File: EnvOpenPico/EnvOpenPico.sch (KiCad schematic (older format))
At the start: 53 parts, among them J2 SKRKAEE020, J3 2.54mm header 01x20, J4 2.54mm header 01x20, J5 Conn_01x03_Male, U1 TPS63002, U3 RP2040, Y1 Crystal

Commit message: added keepout zones around the pins to avoid shorts
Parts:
- Y1: footprint Crystal:Crystal_SMD_5032-2Pin_5.0x3.2mm -> Crystal:Crystal_SMD_3225-4Pin_3.2x2.5mm; symbol Device:Crystal -> Device:Crystal_GND24
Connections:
- wire segments 220 -> 221
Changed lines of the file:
@@
 Connection ~ 3700 5550
 $Comp
-L Device:Crystal Y1
+L Device:Crystal_GND24 Y1
 U 1 1 612055A1
 P 3200 8650
-F 0 "Y1" V 3154 8781 50  0000 L CNN
-F 1 "Crystal" V 3245 8781 50  0000 L CNN
-F 2 "Crystal:Crystal_SMD_5032-2Pin_5.0x3.2mm" H 3200 8650 50  0001 C CNN
+F 0 "Y1" V 3200 8600 50  0000 L CNN
+F 1 "Crystal" V 3400 8700 50  0000 L CNN
+F 2 "Crystal:Crystal_SMD_3225-4Pin_3.2x2.5mm" H 3200 8650 50  0001 C CNN
 F 3 "~" H 3200 8650 50  0001 C CNN
 	1    3200 8650
@@
 	0    -1   -1   0
 $EndComp
-$Comp
-L power:GND #PWR019
-U 1 1 61280CDE
-P 3200 9250
-F 0 "#PWR019" H 3200 9000 50  0001 C CNN
-F 1 "GND" H 3205 9077 50  0000 C CNN
-F 2 "" H 3200 9250 50  0001 C CNN
-F 3 "" H 3200 9250 50  0001 C CNN
-	1    3200 9250
-	1    0    0    -1
-$EndComp
 Wire Wire Line
 	3200 8400 3950 8400
@@
 Wire Wire Line
 	2550 8650 2550 8400
+$Comp
+L power:GND #PWR?
+U 1 1 611FF3FA
+P 3400 8650
+F 0 "#PWR?" H 3400 8400 50  0001 C CNN
+F 1 "GND" V 3405 8522 50  0000 R CNN
+F 2 "" H 3400 8650 50  0001 C CNN
+F 3 "" H 3400 8650 50  0001 C CNN
+	1    3400 8650
+	0    -1   -1   0
+$EndComp
+Wire Wire Line
+	2550 8650 3000 8650
 $EndSCHEMATC

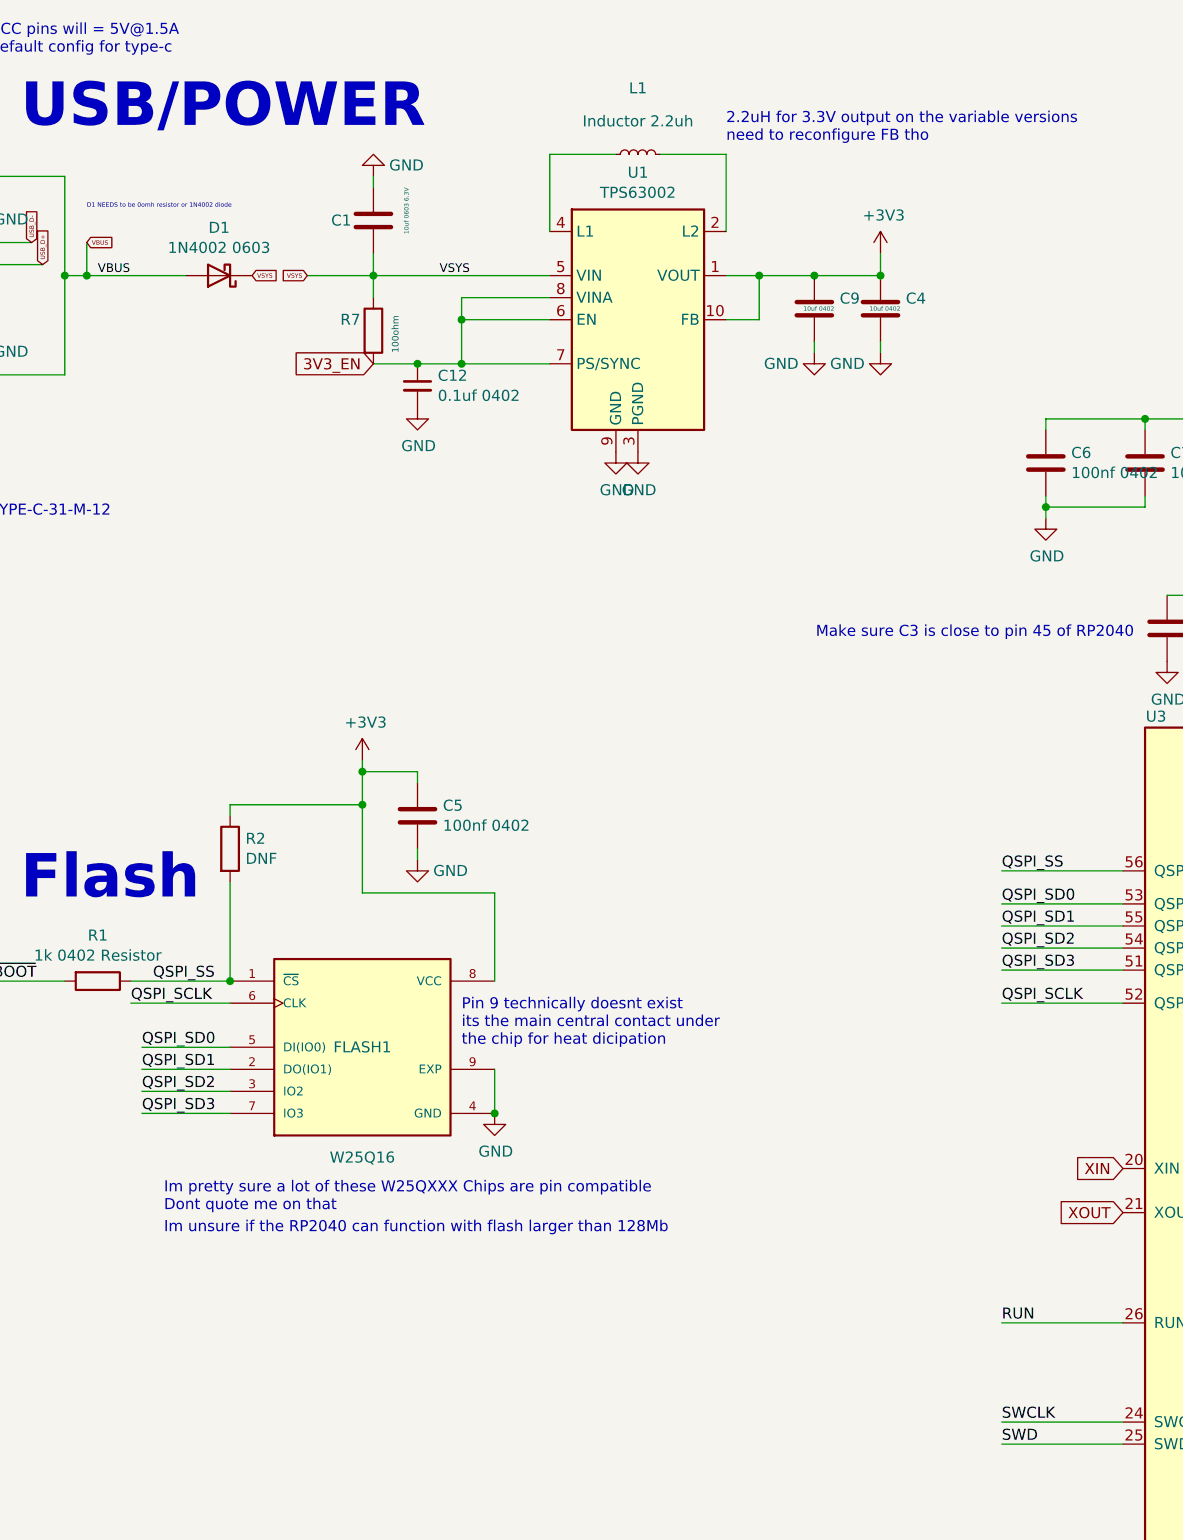
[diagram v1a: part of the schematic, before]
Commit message: Added Reset button + general other tweaks, cleanups and changes.
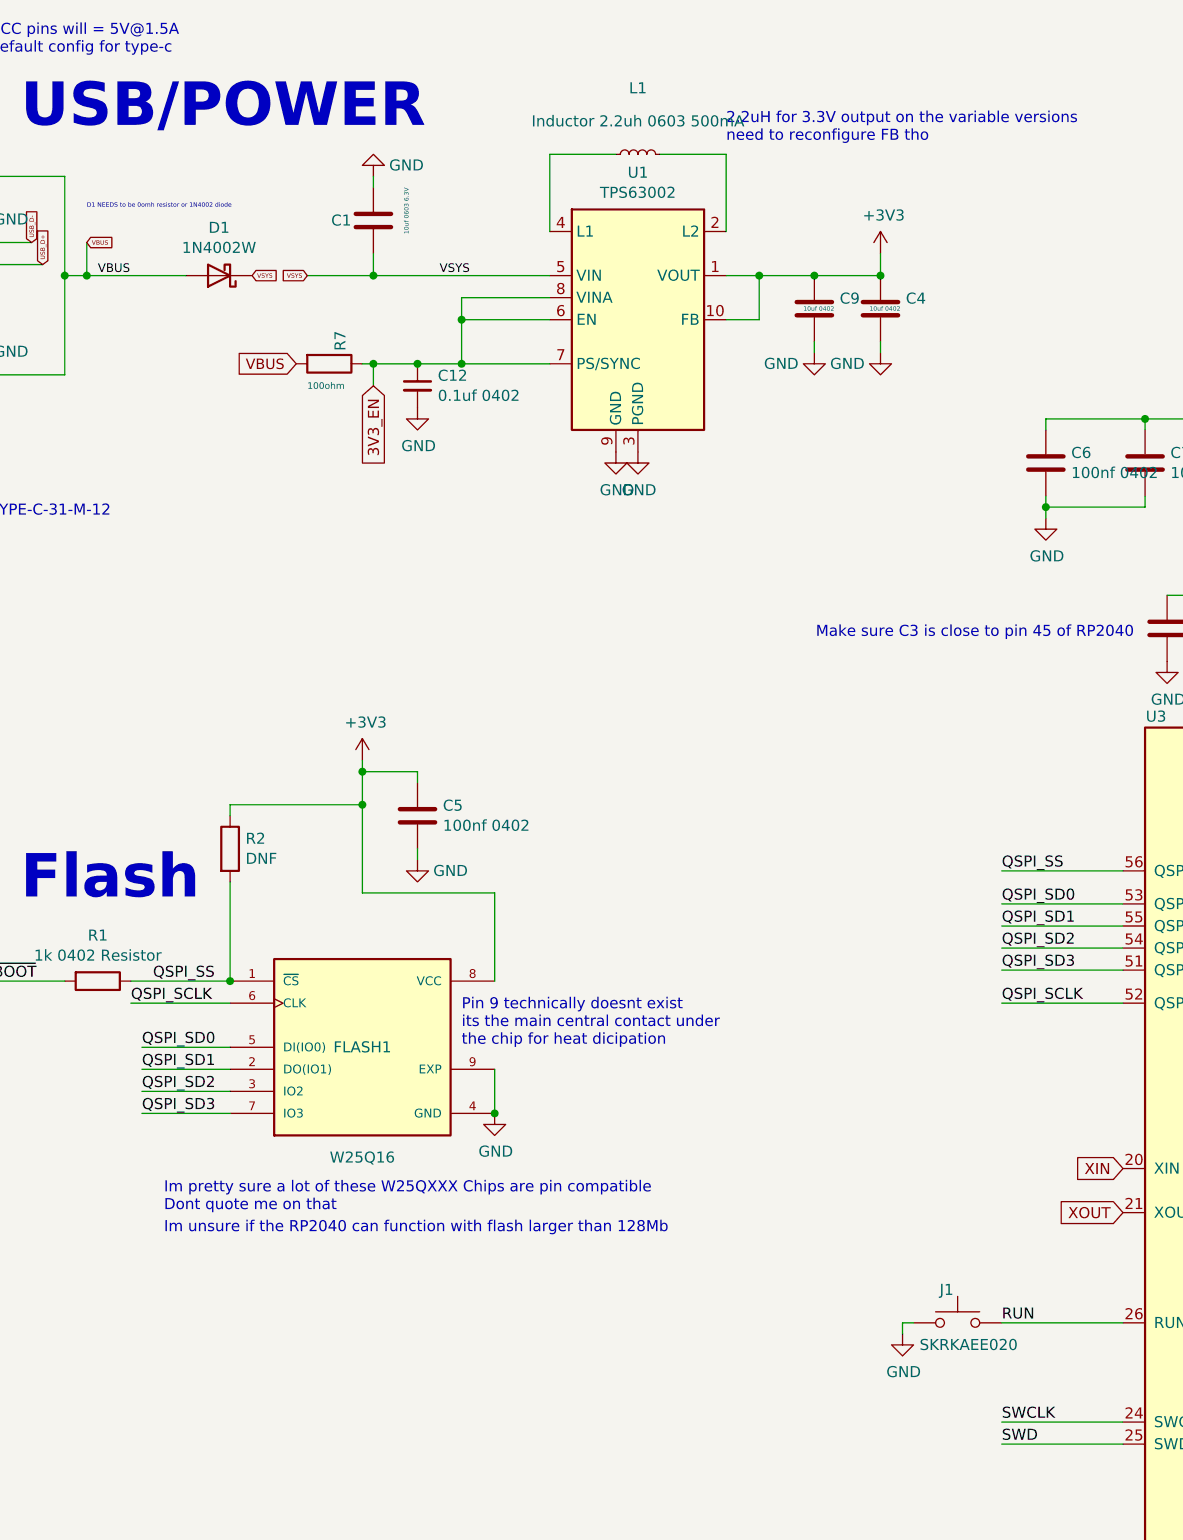
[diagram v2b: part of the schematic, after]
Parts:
- added J1: SKRKAEE020, Button_Switch_SMD:SW_Push_SPST_NO_Alps_SKRK, symbol Switch:SW_Push
- D1: value 1N4002 0603 -> 1N4002W; footprint Diode_SMD:D_0603_1608Metric -> Diode_SMD:D_SOD-123
- L1: value Inductor 2.2uh -> Inductor 2.2uh 0603 500mA; footprint Inductor_SMD:L_0805_2012Metric -> Inductor_SMD:L_0603_1608Metric
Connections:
- net 3V3_EN: now also R7.1; no longer R7.2
- net GND: now also J1.2
- net RUN: now also J1.1
- net VBUS: now also R7.2
- net VSYS: no longer R7.1
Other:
- moved on the sheet: R7
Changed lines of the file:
@@
 Text Notes 600  750  0    50   ~ 0
 2x 5.1K Resistors on the CC pins will = 5V@1.5A\nthis is the recomended default config for type-c
-Text GLabel 3150 2150 0    50   Input ~ 0
+Text GLabel 3150 2250 3    50   Input ~ 0
 3V3_EN
 $Comp
 L Device:R R7
 U 1 1 608CFAF0
-P 3150 2000
-F 0 "R7" H 3000 2050 50  0000 L CNN
-F 1 "100ohm" V 3250 1900 30  0000 L CNN
-F 2 "Resistor_SMD:R_0402_1005Metric" V 3080 2000 50  0001 C CNN
-F 3 "" H 3150 2000 50  0001 C CNN
-	1    3150 2000
-	1    0    0    -1
-$EndComp
-Wire Wire Line
-	3150 1850 3150 1750
+P 2950 2150
+F 0 "R7" H 2800 2200 50  0000 L CNN
+F 1 "100ohm" V 3050 2050 30  0000 L CNN
+F 2 "Resistor_SMD:R_0402_1005Metric" V 2880 2150 50  0001 C CNN
+F 3 "" H 2950 2150 50  0001 C CNN
+	1    2950 2150
+	0    1    1    0
+$EndComp
 $Comp
 L power:GND #PWR0110
@@
 P 4350 1200
 F 0 "L1" V 4650 1200 50  0000 C CNN
-F 1 "Inductor 2.2uh" V 4500 1200 50  0000 C CNN
-F 2 "Inductor_SMD:L_0805_2012Metric" H 4350 1200 50  0001 C CNN
+F 1 "Inductor 2.2uh 0603 500mA" V 4500 1200 50  0000 C CNN
+F 2 "Inductor_SMD:L_0603_1608Metric" H 4350 1200 50  0001 C CNN
 F 3 "~" H 4350 1200 50  0001 C CNN
 	1    4350 1200
@@
 P 2450 1750
 F 0 "D1" H 2450 1533 50  0000 C CNN
-F 1 "1N4002 0603" H 2450 1624 50  0000 C CNN
-F 2 "Diode_SMD:D_0603_1608Metric" H 2450 1750 50  0001 C CNN
+F 1 "1N4002W" H 2450 1624 50  0000 C CNN
+F 2 "Diode_SMD:D_SOD-123" H 2450 1750 50  0001 C CNN
 F 3 "~" H 2450 1750 50  0001 C CNN
 	1    2450 1750
@@
 	2550 8650 2550 8400
 $Comp
-L power:GND #PWR?
+L power:GND #PWR0105
 U 1 1 611FF3FA
 P 3400 8650
-F 0 "#PWR?" H 3400 8400 50  0001 C CNN
+F 0 "#PWR0105" H 3400 8400 50  0001 C CNN
 F 1 "GND" V 3405 8522 50  0000 R CNN
 F 2 "" H 3400 8650 50  0001 C CNN
@@
 Wire Wire Line
 	2550 8650 3000 8650
+Connection ~ 3150 2150
+Wire Wire Line
+	3150 2150 3150 2250
+Wire Wire Line
+	3100 2150 3150 2150
+Text GLabel 2800 2150 0    47   Input ~ 0
+VBUS
+$Comp
+L Switch:SW_Push J1
+U 1 1 61339A7C
+P 5800 6500
+F 0 "J1" H 5850 6650 50  0000 C CNN
+F 1 "SKRKAEE020" H 5750 6400 50  0000 C CNN
+F 2 "Button_Switch_SMD:SW_Push_SPST_NO_Alps_SKRK" H 5800 6500 50  0001 C CNN
+F 3 "" H 5800 6500 50  0001 C CNN
+	1    5800 6500
+	-1   0    0    -1
+$EndComp
+$Comp
+L power:GND #PWR0106
+U 1 1 6133A1A8
+P 5550 6550
+F 0 "#PWR0106" H 5550 6300 50  0001 C CNN
+F 1 "GND" H 5555 6377 50  0000 C CNN
+F 2 "" H 5550 6550 50  0001 C CNN
+F 3 "" H 5550 6550 50  0001 C CNN
+	1    5550 6550
+	1    0    0    -1
+$EndComp
+Wire Wire Line
+	5600 6500 5550 6500
+Wire Wire Line
+	5550 6500 5550 6550
 $EndSCHEMATC

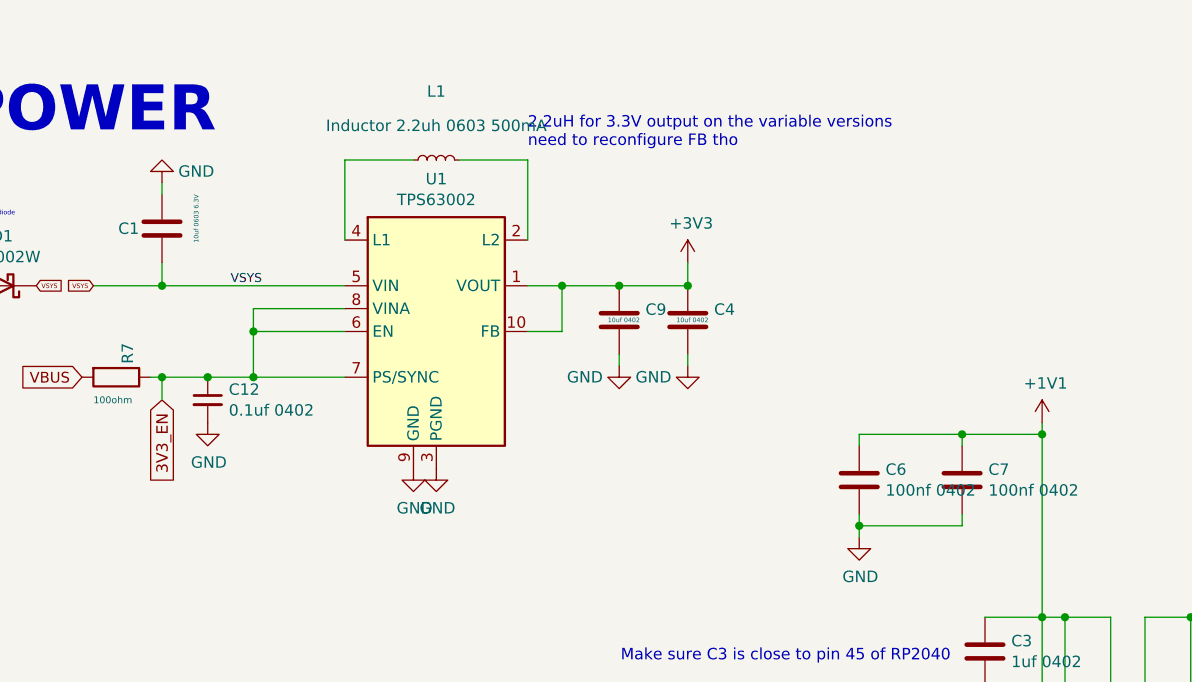
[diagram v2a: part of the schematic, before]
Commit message: Swapped TPS6300x for TLV75533PDBVR due to stock issues.
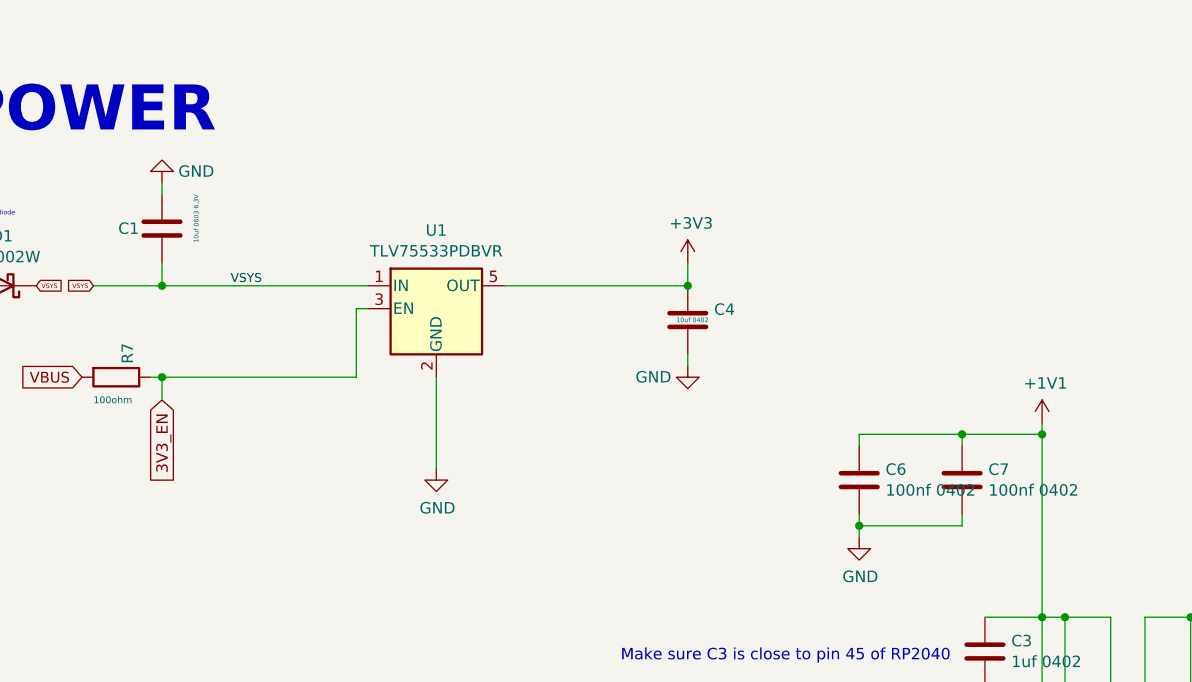
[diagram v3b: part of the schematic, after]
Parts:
- removed C12: 0.1uf 0402, Capacitor_SMD:C_0402_1005Metric, symbol Device:C_Small
- removed C9: 10uf 0402, Capacitor_SMD:C_0402_1005Metric, symbol Device:C
- removed L1: Inductor 2.2uh 0603 500mA, Inductor_SMD:L_0603_1608Metric, symbol Device:L_Small
- removed U1: TPS63002, Package_SON:Texas_DRC0010J_ThermalVias, symbol Regulator_Switching:TPS63002
- added U1: TLV75533PDBVR, Package_TO_SOT_SMD:SOT-23-5, symbol Regulator_Linear:TLV75533PDBV
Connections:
- net +3V3: now also U1.5 (OUT)
- net 3V3_EN: now also U1.3 (EN)
- net GND: now also U1.2 (GND)
- net VSYS: now also U1.1 (IN)
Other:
- note removed: "2.2uH for 3.3V output on the variable versions\nneed to reconfigure FB tho"
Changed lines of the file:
@@
 	0    1    1    0
-$EndComp
-$Comp
-L power:GND #PWR0110
-U 1 1 60C62E0C
-P 4250 2550
-F 0 "#PWR0110" H 4250 2300 50  0001 C CNN
-F 1 "GND" H 4255 2377 50  0000 C CNN
-F 2 "" H 4250 2550 50  0001 C CNN
-F 3 "" H 4250 2550 50  0001 C CNN
-	1    4250 2550
-	1    0    0    -1
-$EndComp
-$Comp
-L power:GND #PWR0111
-U 1 1 60C8A405
-P 3350 2350
-F 0 "#PWR0111" H 3350 2100 50  0001 C CNN
-F 1 "GND" H 3355 2177 50  0000 C CNN
-F 2 "" H 3350 2350 50  0001 C CNN
-F 3 "" H 3350 2350 50  0001 C CNN
-	1    3350 2350
-	1    0    0    -1
-$EndComp
-$Comp
-L Device:L_Small L1
-U 1 1 60C9C176
-P 4350 1200
-F 0 "L1" V 4650 1200 50  0000 C CNN
-F 1 "Inductor 2.2uh 0603 500mA" V 4500 1200 50  0000 C CNN
-F 2 "Inductor_SMD:L_0603_1608Metric" H 4350 1200 50  0001 C CNN
-F 3 "~" H 4350 1200 50  0001 C CNN
-	1    4350 1200
-	0    -1   -1   0
 $EndComp
 Wire Wire Line
@@
 Wire Wire Line
 	14300 5100 14600 5100
-$Comp
-L Regulator_Switching:TPS63002 U1
-U 1 1 60D7C270
-P 4350 1950
-F 0 "U1" H 4350 2617 50  0000 C CNN
-F 1 "TPS63002" H 4350 2526 50  0000 C CNN
-F 2 "Package_SON:Texas_DRC0010J_ThermalVias" H 5200 1400 50  0001 C CNN
-F 3 "http://www.ti.com/lit/ds/symlink/tps63000.pdf" H 4050 2500 50  0001 C CNN
-	1    4350 1950
-	1    0    0    -1
-$EndComp
 Wire Wire Line
 	5450 1650 5450 1750
-Wire Wire Line
-	3950 1550 3950 1200
-Wire Wire Line
-	4750 1550 4750 1200
-Wire Wire Line
-	3550 2150 3550 1950
-Wire Wire Line
-	3550 1850 3950 1850
-Wire Wire Line
-	3150 2150 3350 2150
-Wire Wire Line
-	3950 1950 3550 1950
-Connection ~ 3550 1950
-Wire Wire Line
-	3550 1950 3550 1850
-Wire Wire Line
-	3950 2150 3550 2150
-Connection ~ 3550 2150
-$Comp
-L Device:C_Small C12
-U 1 1 60E73823
-P 3350 2250
-F 0 "C12" H 3442 2296 50  0000 L CNN
-F 1 "0.1uf 0402" H 3442 2205 50  0000 L CNN
-F 2 "Capacitor_SMD:C_0402_1005Metric" H 3350 2250 50  0001 C CNN
-F 3 "~" H 3350 2250 50  0001 C CNN
-	1    3350 2250
-	1    0    0    -1
-$EndComp
-Connection ~ 3350 2150
-Wire Wire Line
-	3350 2150 3550 2150
-$Comp
-L Device:C C9
-U 1 1 60E776B9
-P 5150 1900
-F 0 "C9" H 5265 1946 50  0000 L CNN
-F 1 "10uf 0402" H 5100 1900 20  0000 L CNN
-F 2 "Capacitor_SMD:C_0402_1005Metric" H 5188 1750 50  0001 C CNN
-F 3 "" H 5150 1900 50  0001 C CNN
-	1    5150 1900
-	1    0    0    -1
-$EndComp
-$Comp
-L power:GND #PWR01
-U 1 1 60E776BF
-P 5150 2100
-F 0 "#PWR01" H 5150 1850 50  0001 C CNN
-F 1 "GND" H 5000 2050 50  0000 C CNN
-F 2 "" H 5150 2100 50  0001 C CNN
-F 3 "" H 5150 2100 50  0001 C CNN
-	1    5150 2100
-	1    0    0    -1
-$EndComp
-Wire Wire Line
-	5150 2050 5150 2100
-Wire Wire Line
-	5450 1750 5150 1750
-Connection ~ 5150 1750
 $Comp
 L power:GND #PWR05
@@
 Text Label 14100 5200 0    50   ~ 0
 ADC_VREF
-Wire Wire Line
-	4750 1750 4900 1750
-Wire Wire Line
-	4750 1950 4900 1950
-Wire Wire Line
-	4900 1950 4900 1750
-Connection ~ 4900 1750
-Wire Wire Line
-	4900 1750 5150 1750
 $Comp
 L Device:C C4
@@
 Text Notes 1850 1450 0    20   ~ 0
 D1 NEEDS to be 0omh resistor or 1N4002 diode
-Wire Wire Line
-	3950 1200 4250 1200
-Wire Wire Line
-	4450 1200 4750 1200
-Wire Wire Line
-	3950 1750 3150 1750
 Connection ~ 3150 1750
 Text GLabel 2850 1750 0    20   Input ~ 0
@@
 	0    -1   -1   0
 $EndComp
-Text Notes 4750 1150 0    50   ~ 0
-2.2uH for 3.3V output on the variable versions\nneed to reconfigure FB tho
 Wire Wire Line
 	3700 5550 3700 5350
@@
 Wire Wire Line
 	5550 6500 5550 6550
+$Comp
+L Regulator_Linear:TLV75533PDBV U1
+U 1 1 6128F962
+P 4350 1850
+F 0 "U1" H 4350 2192 50  0000 C CNN
+F 1 "TLV75533PDBVR" H 4350 2101 50  0000 C CNN
+F 2 "Package_TO_SOT_SMD:SOT-23-5" H 4350 2175 50  0001 C CIN
+F 3 "http://www.ti.com/lit/ds/symlink/tlv755p.pdf" H 4350 1900 50  0001 C CNN
+	1    4350 1850
+	1    0    0    -1
+$EndComp
+Wire Wire Line
+	4000 1850 4000 2150
+Wire Wire Line
+	3150 2150 4000 2150
+Wire Wire Line
+	4000 1850 4050 1850
+Wire Wire Line
+	3150 1750 4050 1750
+Wire Wire Line
+	4650 1750 5450 1750
+Wire Wire Line
+	4350 2150 4350 2550
 $EndSCHEMATC
